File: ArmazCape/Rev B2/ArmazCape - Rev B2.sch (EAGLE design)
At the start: 159 parts, among them J2 85505-5113, Q1 32.768kHz, 12.5pF, Q2 ASE, Q4 IRLML6344TRPBF, Q5 IRLML6344TRPBF, U1 L7985A, U12 24AA256-I/SN, U13 L7985A, U4 DS1307ZN+, U5 CD4050BD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

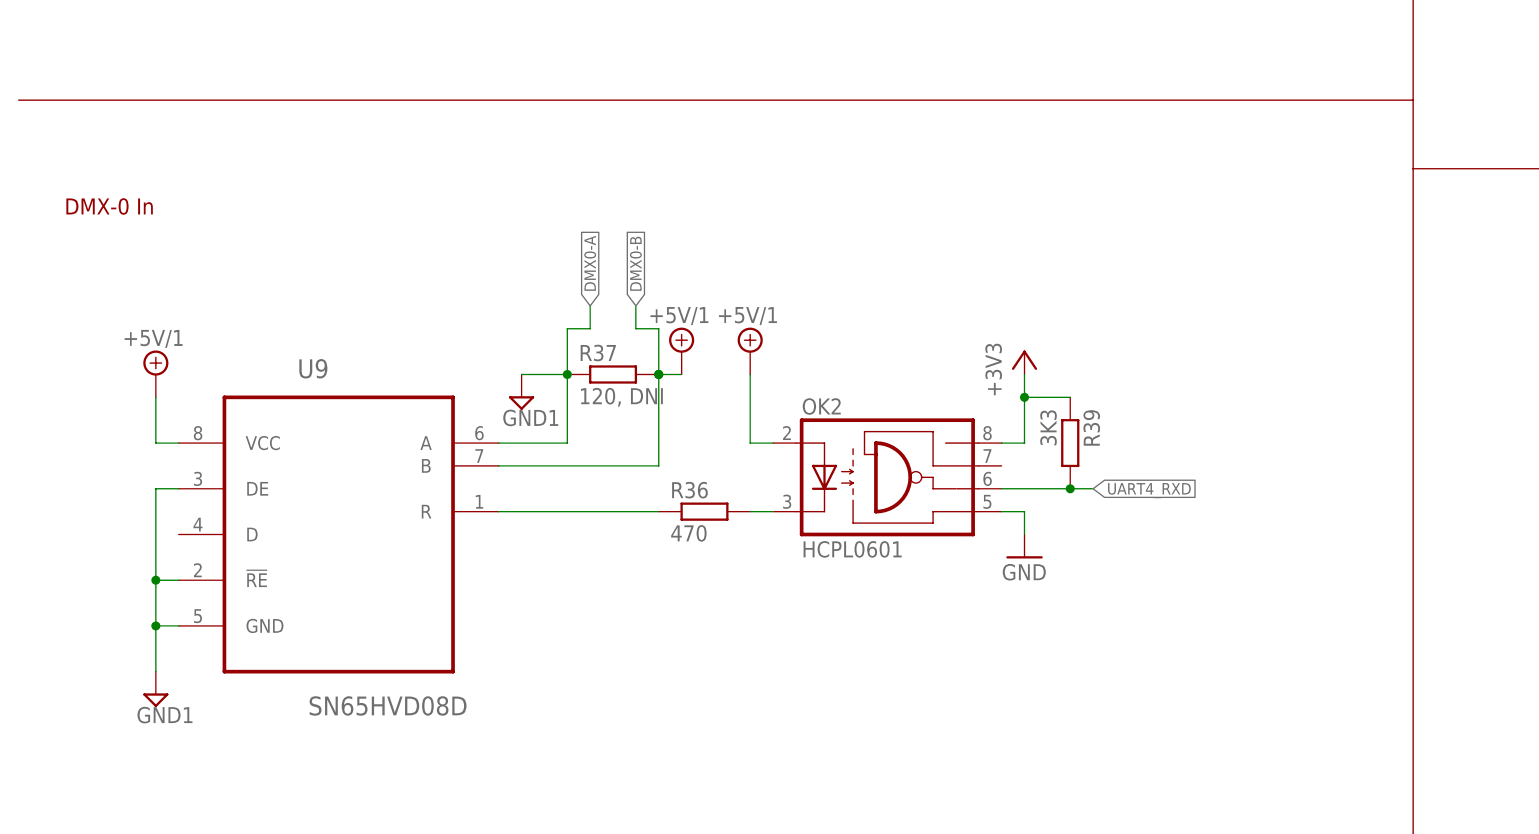
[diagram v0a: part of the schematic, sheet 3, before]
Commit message: Update ArmazCape Rev B2 Schematic, Update 7490100111A chip, Add EMI filter librarie
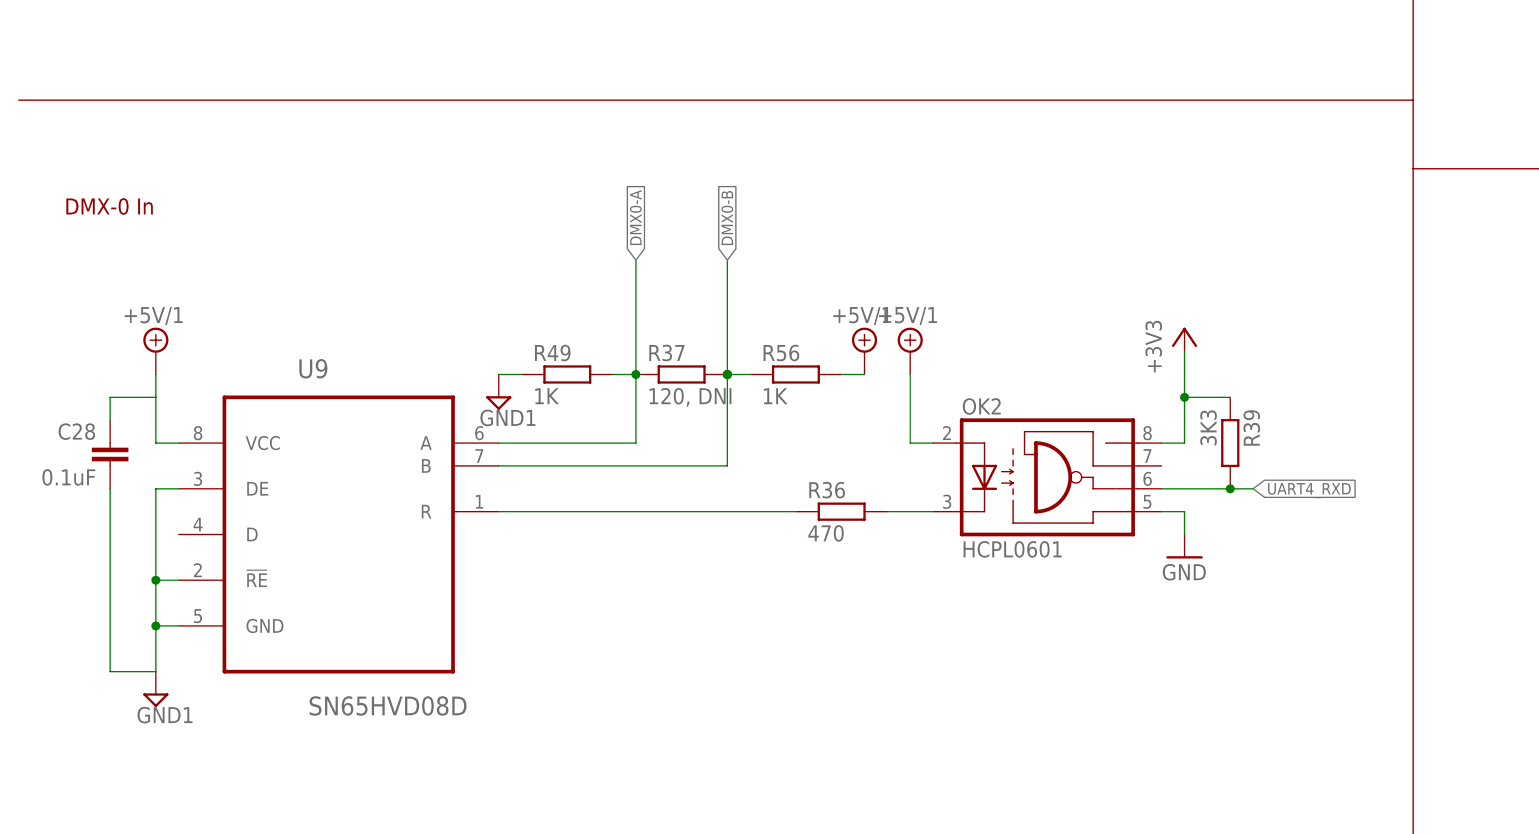
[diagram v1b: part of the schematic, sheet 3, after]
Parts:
- removed L5: 1uH, rcl:L-EUL4532C
- added C23, C34: 4.7uF, rcl:CPOL-EUCT3216
- added C32, C33: 0.1uF, rcl:C-EUC0603
- added R47: 4.7K, rcl:R-EU_R0603
- added R49, R56: 1K, resistor:R-EU_R0603
- added U$6: HI1206N101R-10, emi_filter:HI1206N101R-10
- ISW: OC_FARNELL 9731660 -> (none)
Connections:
- net +3V3: now also Q2.TRI
- net +5V/1: now also C28.1, R56.2
- net DMX0-A: now also R49.2
- net DMX0-B: now also R56.1
- net GND: now also C23.-, C32.2, C33.2, C34.-, R47.1; no longer C28.2
- net GND1: now also C28.2, R49.1
- net N$4: now also R47.2, U$5.EDD_IO; no longer L5.2, U$5.VDD_CO1.8
- net VDD18CORE: now also C23.+, C32.1, C33.1, C34.+, U$5.VDD_CO1.8, U$6.1, U$6.2; no longer C28.1, L5.1
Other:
- note added: "1.8V Filtering"
- moved on the sheet: OK2, Q2, R36, R37, R39

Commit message: Update Armaz schematic Rev B2
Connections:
- new net VDD18PLL: C32.1, C33.1, C34.+, U$5.VDD_A1.8, U$5.VDD_D1.8, U$6.2
- net VDD18CORE: no longer C32.1, C33.1, C34.+, U$5.VDD_A1.8, U$5.VDD_D1.8, U$6.2
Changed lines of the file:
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@@
 </part>
 <part name="GND20" library="supply1" deviceset="GND" device=""/>
-<part name="VDD3V1" library="supply3" deviceset="VDD18CORE" device=""/>
 <part name="VDD3V2" library="supply3" deviceset="VDD18CORE" device=""/>
 <part name="R47" library="rcl" deviceset="R-EU_" device="R0603" value="4.7K">
@@
 </part>
 <part name="VDD3V4" library="supply3" deviceset="VDD18CORE" device=""/>
-<part name="VDD3V5" library="supply3" deviceset="VDD18CORE" device=""/>
 <part name="U$6" library="emi_filter" deviceset="HI1206N101R-10" device="">
 <attribute name="MC" value="LAIRD TECHNOLOGIES"/>
@@
 <attribute name="OC_FARNELL" value="1632391"/>
 </part>
+<part name="U$3" library="supply3" deviceset="VDD18PLL" device=""/>
+<part name="U$7" library="supply3" deviceset="VDD18PLL" device=""/>
 </parts>
 <sheets>
@@
 </instance>
 <instance part="GND20" gate="1" x="167.64" y="78.74"/>
-<instance part="VDD3V1" gate="G$1" x="172.72" y="137.16"/>
 <instance part="VDD3V2" gate="G$1" x="165.1" y="137.16"/>
 <instance part="R47" gate="G$1" x="241.3" y="116.84" rot="R90">
@@
 <instance part="+3V12" gate="G$1" x="259.08" y="40.64"/>
 <instance part="VDD3V4" gate="G$1" x="152.4" y="35.56"/>
-<instance part="VDD3V5" gate="G$1" x="200.66" y="35.56"/>
 <instance part="U$6" gate="FB$1" x="165.1" y="27.94">
 <attribute name="MC" x="165.1" y="27.94" size="1.778" layer="96" display="off"/>
@@
 <attribute name="OC_FARNELL" x="182.88" y="25.4" size="1.778" layer="96" display="off"/>
 </instance>
+<instance part="U$3" gate="G$1" x="200.66" y="35.56"/>
+<instance part="U$7" gate="G$1" x="172.72" y="137.16"/>
 </instances>
 <busses>
@@
 <wire x1="114.3" y1="139.7" x2="114.3" y2="137.16" width="0.1524" layer="91"/>
 <pinref part="D4" gate="A" pin="A"/>
+<junction x="106.68" y="139.7"/>
 </segment>
 <segment>
@@
 <wire x1="119.38" y1="68.58" x2="119.38" y2="66.04" width="0.1524" layer="91"/>
 <pinref part="D3" gate="A" pin="A"/>
+<junction x="111.76" y="68.58"/>
 </segment>
 <segment>
@@
 <junction x="190.5" y="20.32"/>
 <wire x1="190.5" y1="20.32" x2="182.88" y2="20.32" width="0.1524" layer="91"/>
+<junction x="182.88" y="20.32"/>
 </segment>
 </net>
@@
 <net name="VDD18CORE" class="0">
 <segment>
-<pinref part="VDD3V1" gate="G$1" pin="VDD18CORE"/>
-<pinref part="U$5" gate="G$1" pin="VDD_A1.8"/>
-<wire x1="172.72" y1="134.62" x2="172.72" y2="121.92" width="0.1524" layer="91"/>
-<wire x1="172.72" y1="121.92" x2="180.34" y2="121.92" width="0.1524" layer="91"/>
-<pinref part="U$5" gate="G$1" pin="VDD_D1.8"/>
-<wire x1="180.34" y1="121.92" x2="182.88" y2="121.92" width="0.1524" layer="91"/>
-<wire x1="180.34" y1="121.92" x2="180.34" y2="119.38" width="0.1524" layer="91"/>
-<wire x1="180.34" y1="119.38" x2="182.88" y2="119.38" width="0.1524" layer="91"/>
-<junction x="180.34" y="121.92"/>
-</segment>
-<segment>
 <pinref part="VDD3V2" gate="G$1" pin="VDD18CORE"/>
 <pinref part="U$5" gate="G$1" pin="VDD_CO1.8"/>
@@
 <wire x1="152.4" y1="27.94" x2="160.02" y2="27.94" width="0.1524" layer="91"/>
 </segment>
-<segment>
-<pinref part="U$6" gate="FB$1" pin="2"/>
-<pinref part="C33" gate="G$1" pin="1"/>
-<wire x1="170.18" y1="27.94" x2="182.88" y2="27.94" width="0.1524" layer="91"/>
-<pinref part="VDD3V5" gate="G$1" pin="VDD18CORE"/>
-<wire x1="182.88" y1="27.94" x2="190.5" y2="27.94" width="0.1524" layer="91"/>
-<wire x1="190.5" y1="27.94" x2="200.66" y2="27.94" width="0.1524" layer="91"/>
-<wire x1="200.66" y1="27.94" x2="200.66" y2="33.02" width="0.1524" layer="91"/>
-<pinref part="C32" gate="G$1" pin="1"/>
-<junction x="190.5" y="27.94"/>
-<pinref part="C34" gate="G$1" pin="+"/>
-<junction x="182.88" y="27.94"/>
-</segment>
 </net>
 <net name="SYS_RESET" class="0">
@@
 </segment>
 </net>
+<net name="VDD18PLL" class="0">
+<segment>
+<pinref part="U$6" gate="FB$1" pin="2"/>
+<pinref part="C33" gate="G$1" pin="1"/>
+<wire x1="170.18" y1="27.94" x2="182.88" y2="27.94" width="0.1524" layer="91"/>
+<wire x1="182.88" y1="27.94" x2="190.5" y2="27.94" width="0.1524" layer="91"/>
+<wire x1="190.5" y1="27.94" x2="200.66" y2="27.94" width="0.1524" layer="91"/>
+<wire x1="200.66" y1="27.94" x2="200.66" y2="33.02" width="0.1524" layer="91"/>
+<pinref part="C32" gate="G$1" pin="1"/>
+<junction x="190.5" y="27.94"/>
+<pinref part="C34" gate="G$1" pin="+"/>
+<junction x="182.88" y="27.94"/>
+<pinref part="U$3" gate="G$1" pin="VDD18PLL"/>
+</segment>
+<segment>
+<pinref part="U$5" gate="G$1" pin="VDD_A1.8"/>
+<wire x1="172.72" y1="121.92" x2="180.34" y2="121.92" width="0.1524" layer="91"/>
+<pinref part="U$5" gate="G$1" pin="VDD_D1.8"/>
+<wire x1="180.34" y1="121.92" x2="182.88" y2="121.92" width="0.1524" layer="91"/>
+<wire x1="180.34" y1="121.92" x2="180.34" y2="119.38" width="0.1524" layer="91"/>
+<wire x1="180.34" y1="119.38" x2="182.88" y2="119.38" width="0.1524" layer="91"/>
+<junction x="180.34" y="121.92"/>
+<pinref part="U$7" gate="G$1" pin="VDD18PLL"/>
+<wire x1="172.72" y1="121.92" x2="172.72" y2="134.62" width="0.1524" layer="91"/>
+</segment>
+</net>
 </nets>
 </sheet>
@@
 <wire x1="15.24" y1="45.72" x2="15.24" y2="25.4" width="0.1524" layer="91"/>
 <wire x1="15.24" y1="25.4" x2="20.32" y2="25.4" width="0.1524" layer="91"/>
+<junction x="20.32" y="25.4"/>
 </segment>
 <segment>
@@
 <wire x1="15.24" y1="53.34" x2="15.24" y2="55.88" width="0.1524" layer="91"/>
 <wire x1="15.24" y1="55.88" x2="20.32" y2="55.88" width="0.1524" layer="91"/>
+<junction x="20.32" y="55.88"/>
 </segment>
 <segment>

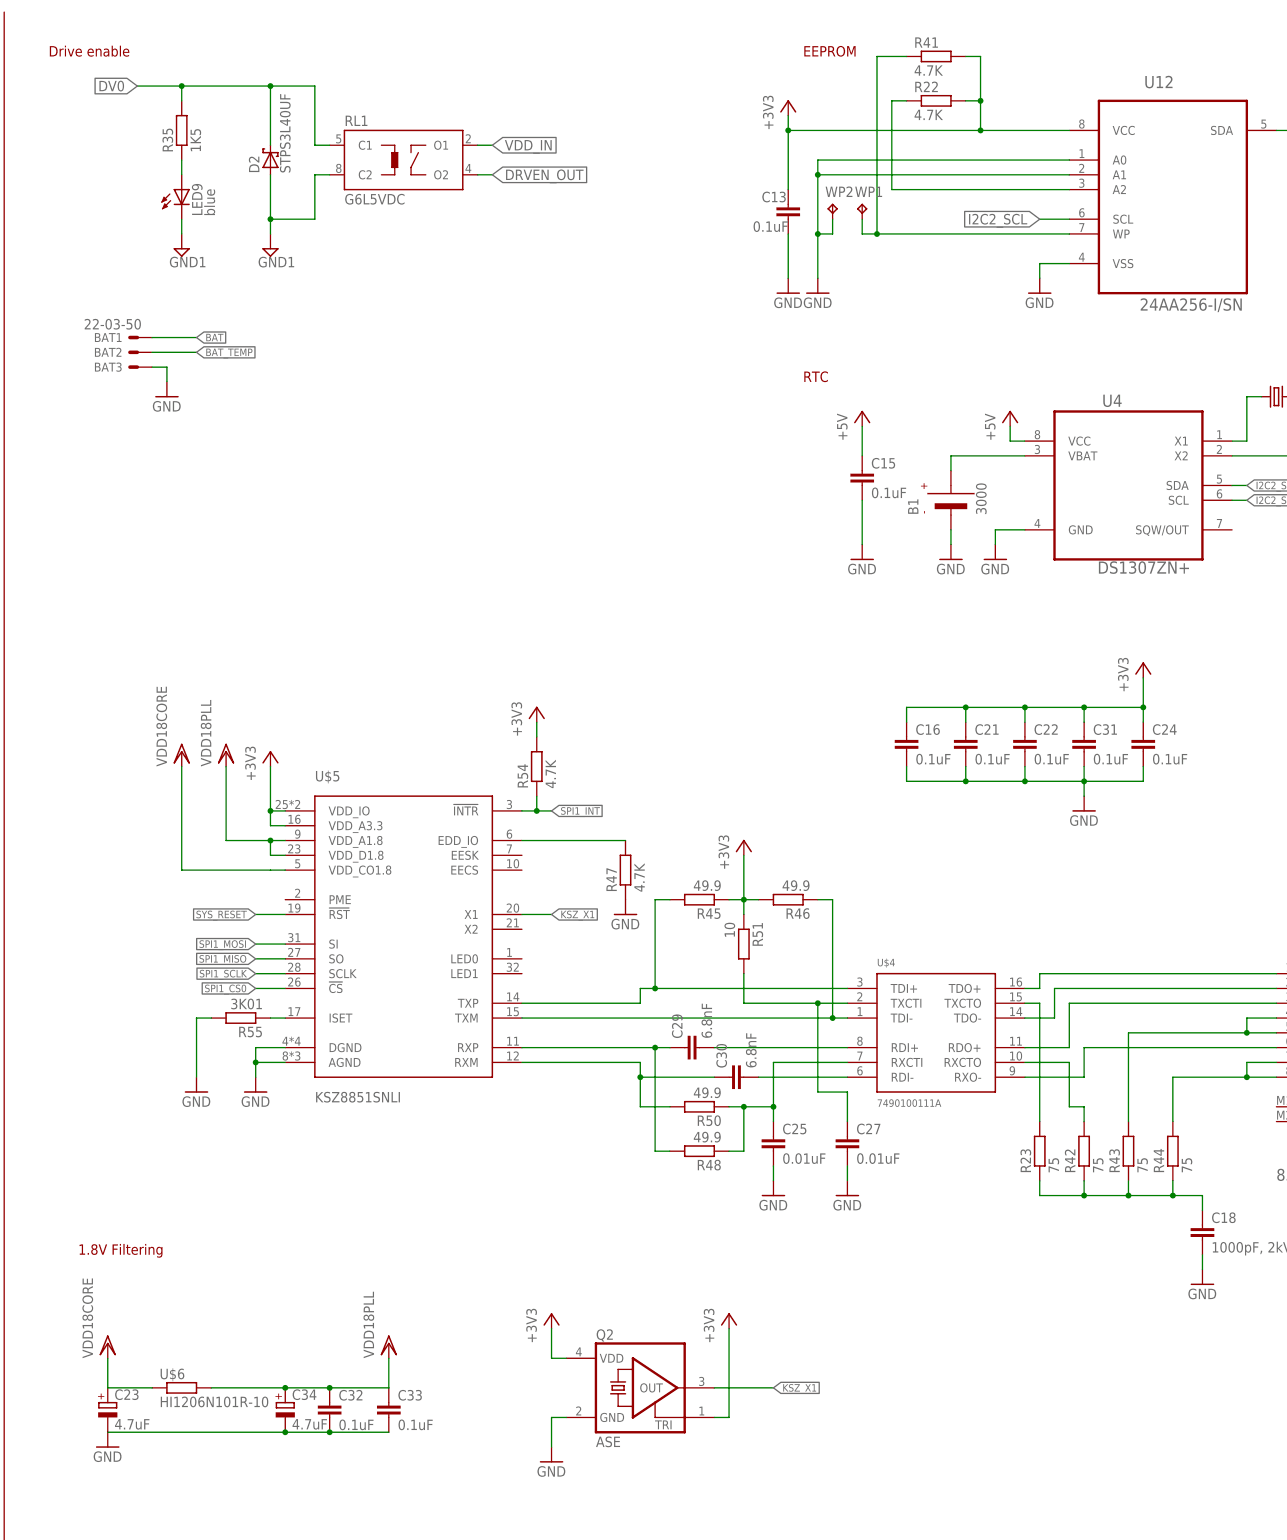
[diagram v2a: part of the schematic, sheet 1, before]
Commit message: Repaired ArmazCape - Rev B2
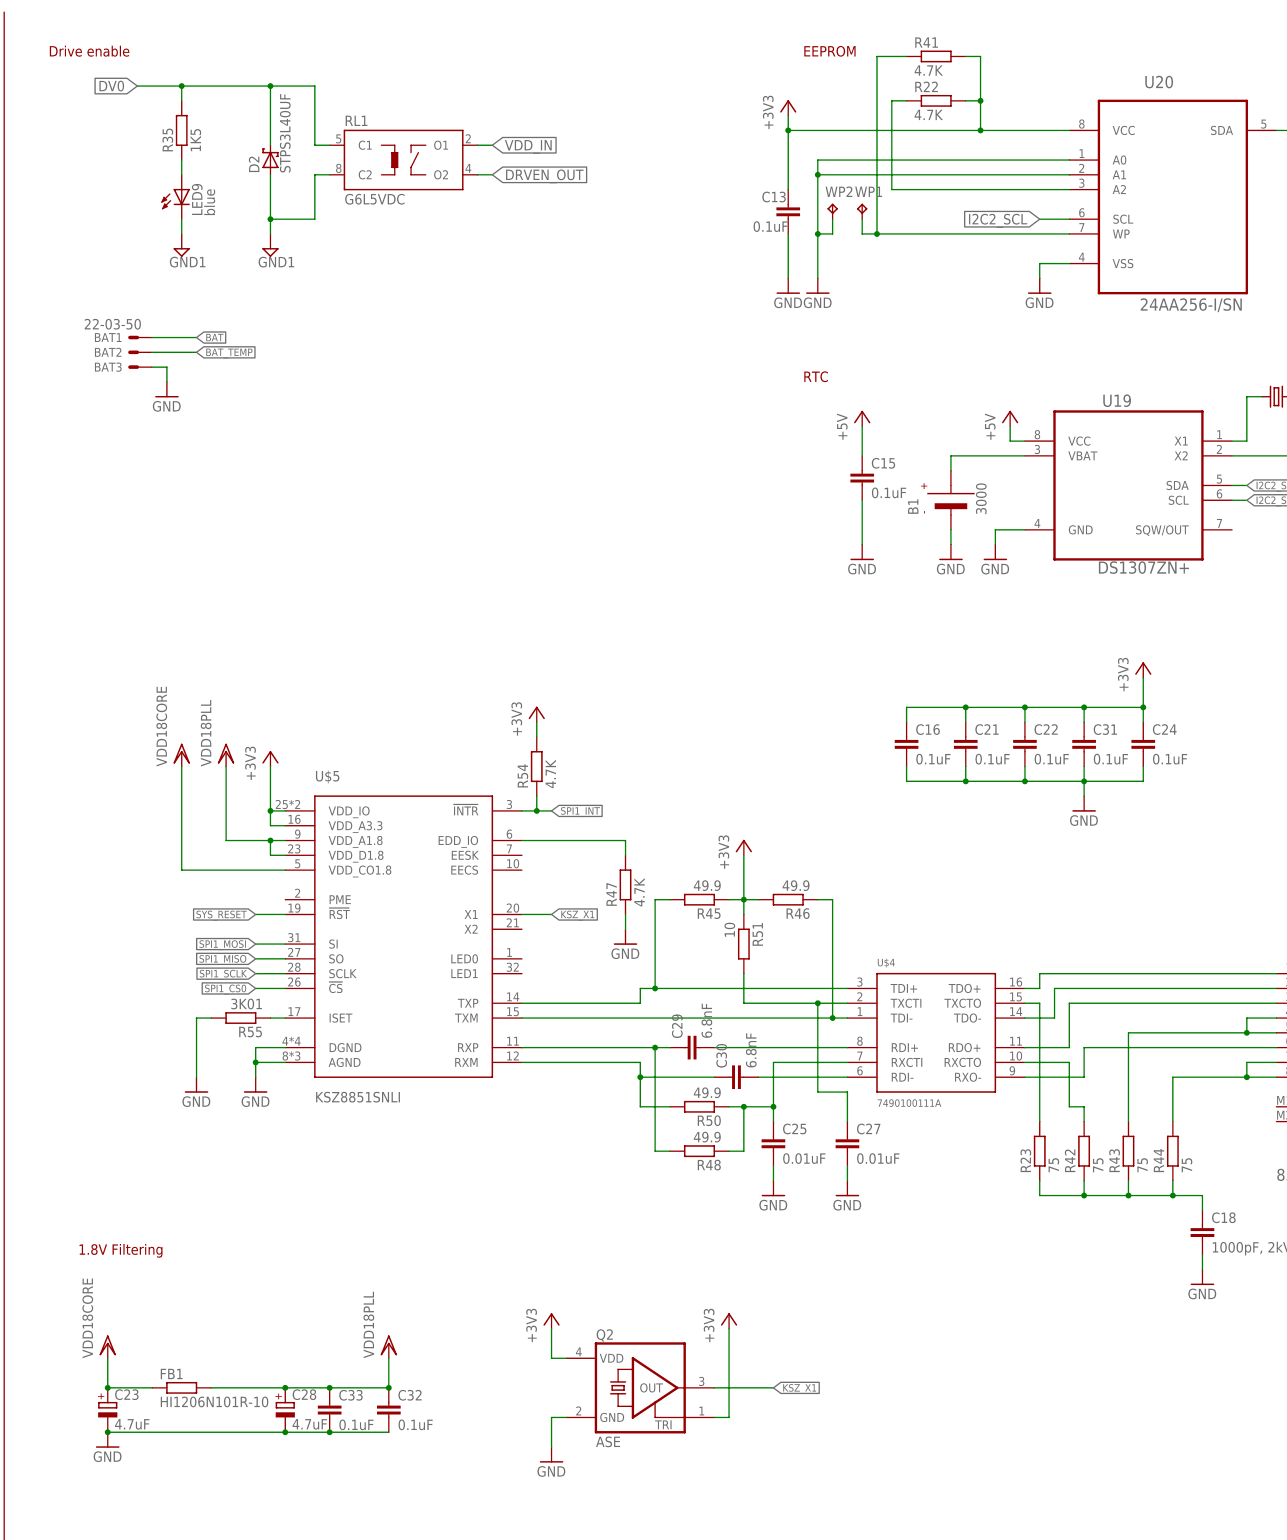
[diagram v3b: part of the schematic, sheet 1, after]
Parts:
- removed U12: 24AA256-I/SN, Microchip_By_element14_Batch_1:24AA256-I/SN
- removed U4: DS1307ZN+, maxim:DS1307ZN+
- added U19: DS1307ZN+, ArmazCape - Rev B2:MAXIM_DS1307ZN+
- added U20: 24AA256-I/SN, ArmazCape - Rev B2:MICROCHIP_BY_ELEMENT14_BATCH_1_24AA256-I/SN
- C23: MF AVX -> AVX (FORMERLY KNOWN AS NICHICON)
- C28: value 0.1uF -> 4.7uF; device rcl:C-EUC0603 -> rcl:CPOL-EUCT3216; MF MULTICOMP -> AVX (FORMERLY KNOWN AS NICHICON); MPN MC0603B104K250CT -> F931A475MAA; OC_FARNELL 1759037 -> 1818579
- C34: value 4.7uF -> 0.1uF; device rcl:CPOL-EUCT3216 -> rcl:C-EUC0603; MPN F931A475MAA -> MC0603B104K250CT; OC_FARNELL 1818579 -> 1759037
- FB1: MC LAIRD TECHNOLOGIES -> (none); MF (none) -> LAIRD TECHNOLOGIES; MPN HI1206N101R-10 -> (none); OC_FARNELL 2292367 -> (none)
- ISW: OC_FARNELL (none) -> 9731660
- R49, R56: value 1K -> 1k; device resistor:R-EU_R0603 -> rcl-2:R-EUR0603; MPN MC0603SAF1001T5E -> MCMR06X1001FTL; OC_FARNELL 1632391 -> 2073348
- U$5: MF (none) -> MICREL SEMICONDUCTOR; MPN (none) -> KSZ8851SNLI TR; OC_FARNELL (none) -> 1961911
- renumbered U$6 to FB1
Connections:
- net TD+ renamed N$4200
- net TD- renamed N$4400
- net +3V3: now also U20.VCC; no longer U12.VCC
- net +5V: now also U19.VCC; no longer U4.VCC
- net +5V/1: now also C34.1, R56.1; no longer C28.1, R56.2
- net DMX0-A: now also R49.1; no longer R49.2
- net DMX0-B: now also R56.2; no longer R56.1
- net GND: now also C28.-, U19.GND, U20.A0, U20.A1, U20.VSS; no longer C34.-, U12.A0, U12.A1, U12.VSS, U4.GND
- net GND1: now also C34.2, R49.2; no longer C28.2, R49.1
- net I2C2_SCL: now also U19.SCL, U20.SCL; no longer U12.SCL, U4.SCL
- net I2C2_SDA: now also U19.SDA, U20.SDA; no longer U12.SDA, U4.SDA
- net N$24: now also U19.X1; no longer U4.X1
- net N$26: now also U19.X2; no longer U4.X2
- net N$34: now also U20.WP; no longer U12.WP
- net N$35: now also U20.A2; no longer U12.A2
- net VBAT+: now also U19.VBAT; no longer U4.VBAT
- net VDD18PLL: now also C28.+; no longer C34.+
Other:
- moved on the sheet: C32, C33, R47, R49, R56
